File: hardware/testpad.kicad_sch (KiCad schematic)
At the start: 51 parts, among them J1 HC-TYPE-C-16P-CB1.6, J3 AFA01-S08FCA-00, SW1 SSSS811101, SW2 SC4823S6-TR, SW3 SC4823S6-TR, SW4 SC4823S6-TR, SW5 SC4823S6-TR, T1 XL4067TS, U1 ESP32-C6-WROOM-1-N8, U2 BQ24074RGTR, U3 TLA2518IRTER, U6 TPS62142RGTR

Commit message: :bug: improve hardware design
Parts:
- removed R2, R4: 4.7kΩ, KeysDock:R_0402, symbol components:0402,4.7kΩ
- added C12: 1uF, KeysDock:C_0402, symbol components:0402,1uF
- added C13: 100nF, KeysDock:C_0402, symbol components:0402,100nF
- added R15, R16, R18, R25: 10kΩ, KeysDock:R_0402, symbol components:0402,10kΩ
- added R17, R19, R20, R21, R26, R27: 100kΩ, KeysDock:R_0402, symbol components:0402,100kΩ
- added R2, R4: 5.1kΩ, KeysDock:R_0402, symbol components:0402,5.1kΩ
- added R22, R23: 22Ω, KeysDock:R_0402, symbol components:0402,22Ω
- added R24: 47kΩ, KeysDock:R_0402, symbol components:0402,47kΩ
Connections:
- net BAT_CHG: now also R17.2
- net BOOT_0: now also R25.2
- net BOOT_1: now also R16.2
- net EN: now also C12.1, R15.2
- net P,+3.3: now also R15.1, R16.1, R17.1, R18.1, R25.1, R26.1; no longer T1.16 (Y15), T1.17 (Y14), T1.18 (Y13), T1.19 (Y12), T1.2 (Y7), T1.20 (Y11), T1.21 (Y10), T1.22 (Y9), T1.23 (Y8), T1.3 (Y6), T1.4 (Y5), T1.5 (Y4), U3.2 (AIN3/GPIO3), U3.3 (AIN4/GPIO4), U3.4 (AIN5/GPIO5), U3.5 (AIN6/GPIO6)
- net P,E: now also C12.2, R19.2, R2.2, R24.1, R4.2; no longer U2.14 (TMR)
- net P,GND: now also C13.2, R21.1, R27.2
- net RANA: now also R19.1
- net SAKI_MOVE: now also R18.2
- net USB_D+: now also R22.2; no longer J1.A6 (D+), J1.B6 (D+)
- net USB_D-: now also R23.2; no longer J1.A7 (D-), J1.B7 (D-)
- net VBAT: now also R20.1; no longer U3.6 (AIN7/GPIO7)
- net BAT_PGOOD: now reaches U2.7 (~{PGOOD})
- net BAT_PGOOD: now also U1.4 (MTMS/GPIO4/ADC1_CH4)
- net at J1.A5 (CC1): now also R4.1
- net at J1.B5 (CC2): now also R2.1
- new net: R24.2, U2.14 (TMR)
- new net: C13.1, R20.2, R21.2, U3.6 (AIN7/GPIO7)
- new net: J1.A6 (D+), J1.B6 (D+), R22.1
- new net: J1.A7 (D-), J1.B7 (D-), R23.1
- new net KEYS_DT_OTHER: R26.2, R27.1, T1.16 (Y15), T1.17 (Y14), T1.18 (Y13), T1.19 (Y12), T1.2 (Y7), T1.20 (Y11), T1.21 (Y10), T1.22 (Y9), T1.23 (Y8), T1.3 (Y6), T1.4 (Y5), T1.5 (Y4), U3.2 (AIN3/GPIO3), U3.3 (AIN4/GPIO4), U3.4 (AIN5/GPIO5), U3.5 (AIN6/GPIO6)
- no-connect marks 5 -> 3
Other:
- moved on the sheet: LED2, LED3, LED4, LED5, R14, T1

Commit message: :sparkles: sync testpad
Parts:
- removed R17: 100kΩ, KeysDock:R_0402, symbol components:0402,100kΩ
- removed R25: 10kΩ, KeysDock:R_0402, symbol components:0402,10kΩ
- added D2: TPD1E10B06DPYR, KeysDock:DIO_TPD1E05U06DPYR, symbol components:TPD1E10B06DPYR
- added R17, R25: 1.5kΩ, KeysDock:R_0402, symbol components:0402,1.5kΩ
- added R28: 10kΩ, KeysDock:R_0402, symbol components:0402,10kΩ
- added U4: TPD4E05U06DQAR, KeysDock:IC_TPD4E05U06DQAR, symbol components:TPD4E05U06DQAR
- L1: value 2.2uH,5mA -> 2.2uH,3A
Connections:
- net BAT_CHG: now also R17.2
- net BAT_PGOOD: now also R25.2
- net BOOT_0: now also R28.2
- net P,+3.3: now also R28.1
- net P,+5: now also R17.1, R25.1
- net USB_PWR_SUPP: now also D2.1
- net at J1.B5 (CC2), R2.1: now also U4.5 (D2-)
- net at J1.A5 (CC1), R4.1: now also U4.1 (D1+)
- net at J1.A6 (D+), J1.B6 (D+), R22.1: now also U4.10 (NC_10), U4.2 (D1-), U4.9 (NC_9)
- net at J1.A7 (D-), J1.B7 (D-), R23.1: now also U4.4 (D2+), U4.6 (NC_6), U4.7 (NC_7)
- net P,E renamed GND
- net GND: now also D2.2, U4.3 (GND), U4.8 (GND)
- no-connect marks 3 -> 5
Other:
- moved on the sheet: LED2, LED3, LED4, LED5, R14, R26, R27, T1

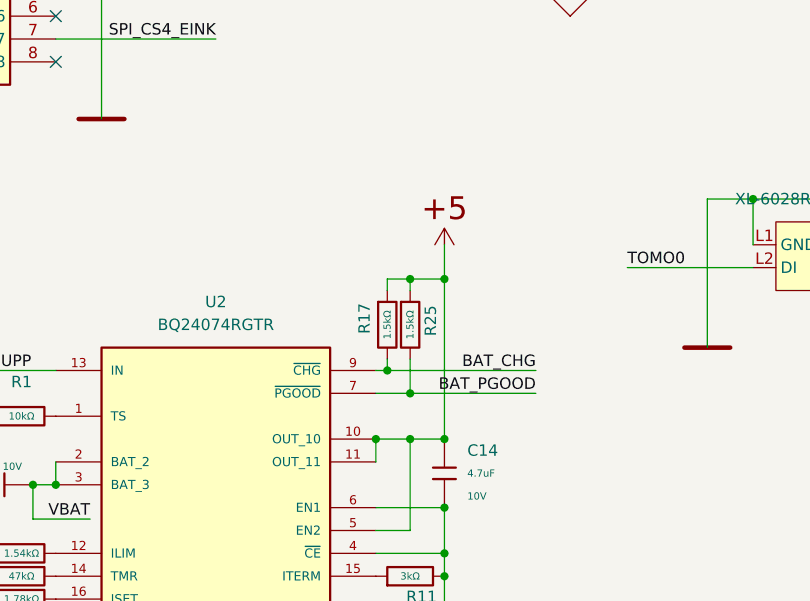
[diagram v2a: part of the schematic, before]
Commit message: :zap: improve led power supply
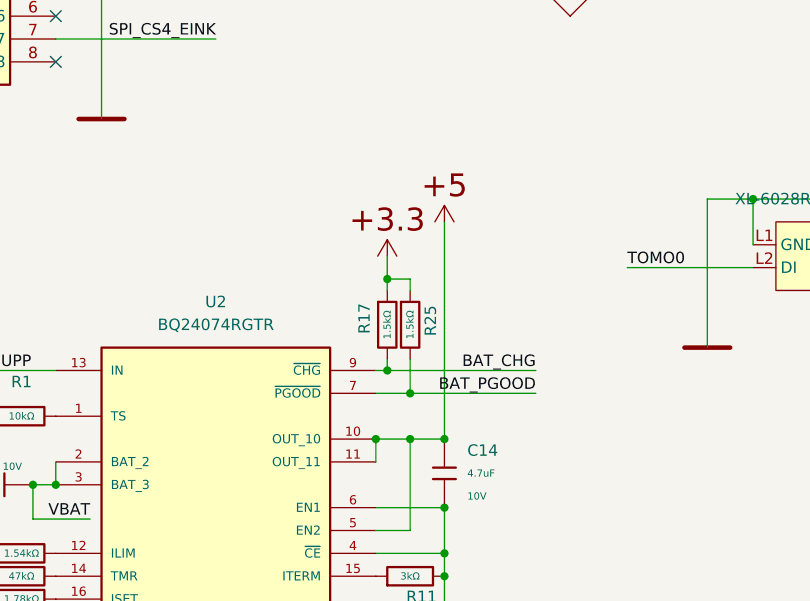
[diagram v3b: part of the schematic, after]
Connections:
- net P,+3.3: now also R17.1, R25.1
- net P,+5: no longer R17.1, R25.1
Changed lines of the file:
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@@
 	)
 	(junction
+		(at 242.57 219.71)
+		(diameter 0)
+		(color 0 0 0 0)
+	)
+	(junction
 		(at 148.59 208.28)
 		(diameter 0)
@@
 	)
 	(junction
+		(at 248.92 237.49)
+		(diameter 0)
+		(color 0 0 0 0)
+	)
+	(junction
 		(at 71.12 222.25)
 		(diameter 0)
@@
 	)
 	(junction
-		(at 248.92 219.71)
-		(diameter 0)
-		(color 0 0 0 0)
-	)
-	(junction
 		(at 151.13 27.94)
 		(diameter 0)
@@
 	)
 	(junction
-		(at 248.92 237.49)
-		(diameter 0)
-		(color 0 0 0 0)
-	)
-	(junction
 		(at 120.65 203.2)
 		(diameter 0)
@@
 	)
 	(junction
-		(at 245.11 219.71)
-		(diameter 0)
-		(color 0 0 0 0)
-	)
-	(junction
 		(at 55.88 233.68)
 		(diameter 0)
@@
 	(wire
 		(pts
-			(xy 245.11 219.71) (xy 248.92 219.71)
-		)
-		(stroke
-			(width 0)
-			(type default)
-		)
-	)
-	(wire
-		(pts
 			(xy 269.24 218.44) (xy 283.21 218.44)
 		)
@@
 	(wire
 		(pts
-			(xy 248.92 215.9) (xy 248.92 219.71)
+			(xy 139.7 76.2) (xy 157.48 76.2)
 		)
 		(stroke
@@
 	(wire
 		(pts
-			(xy 139.7 76.2) (xy 157.48 76.2)
+			(xy 248.92 213.36) (xy 248.92 237.49)
 		)
 		(stroke
@@
 	(wire
 		(pts
-			(xy 248.92 219.71) (xy 248.92 237.49)
+			(xy 226.06 161.29) (xy 231.14 161.29)
 		)
 		(stroke
@@
 	(wire
 		(pts
-			(xy 226.06 161.29) (xy 231.14 161.29)
+			(xy 242.57 217.17) (xy 242.57 219.71)
 		)
 		(stroke
@@
 	)
 	(symbol
+		(lib_id "PCM_Generic:P,+3.3")
+		(at 242.57 217.17 0)
+		(unit 1)
+		(body_style 1)
+		(exclude_from_sim no)
+		(in_bom yes)
+		(on_board yes)
+		(in_pos_files yes)
+		(dnp no)
+		(fields_autoplaced yes)
+		(property "Reference" "#PWR057"
+			(at 245.11 217.17 0)
+			(hide yes)
+			(show_name no)
+			(do_not_autoplace no)
+			(effects
+				(font
+					(size 2.54 2.54)
+				)
+				(justify left)
+			)
+		)
+		(property "Value" "P,+3.3"
+			(at 242.57 214.63 0)
+			(hide yes)
+			(show_name no)
+			(do_not_autoplace no)
+			(effects
+				(font
+					(size 0.001 0.001)
+				)
+				(justify bottom)
+			)
+		)
+		(property "Footprint" ""
+			(at 242.57 217.17 0)
+			(hide yes)
+			(show_name no)
+			(do_not_autoplace no)
+			(effects
+				(font
+					(size 2.54 2.54)
+				)
+			)
+		)
+		(property "Datasheet" ""
+			(at 242.57 217.17 0)
+			(hide yes)
+			(show_name no)
+			(do_not_autoplace no)
+			(effects
+				(font
+					(size 2.54 2.54)
+				)
+			)
+		)
+		(property "Description" "+3.3 positive potential/voltage (global DC power supply node)"
+			(at 242.57 217.17 0)
+			(hide yes)
+			(show_name no)
+			(do_not_autoplace no)
+			(effects
+				(font
+					(size 1.27 1.27)
+				)
+			)
+		)
+		(pin "0"
+		)
+		(instances
+			(project "testpad"
+				(path "/4162c9f0-7325-4010-974e-29020dac9fdc"
+					(reference "#PWR057")
+					(unit 1)
+				)
+			)
+		)
+	)
+	(symbol
 		(lib_id "components:EC12E1240301")
 		(at 168.91 38.1 270)
@@
 	(symbol
 		(lib_id "PCM_Generic:P,+5")
-		(at 248.92 215.9 0)
+		(at 248.92 213.36 0)
 		(unit 1)
 		(body_style 1)
@@
 		(fields_autoplaced yes)
 		(property "Reference" "#PWR031"
-			(at 251.46 215.9 0)
+			(at 251.46 213.36 0)
 			(hide yes)
 			(show_name no)
@@
 		)
 		(property "Value" "P,+5"
-			(at 248.92 213.36 0)
+			(at 248.92 210.82 0)
 			(hide yes)
 			(show_name no)
@@
 		)
 		(property "Footprint" ""
-			(at 248.92 215.9 0)
+			(at 248.92 213.36 0)
 			(hide yes)
 			(show_name no)
@@
 		)
 		(property "Datasheet" ""
-			(at 248.92 215.9 0)
+			(at 248.92 213.36 0)
 			(hide yes)
 			(show_name no)
@@
 		)
 		(property "Description" "+5 positive potential/voltage (global DC power supply node)"
-			(at 248.92 215.9 0)
+			(at 248.92 213.36 0)
 			(hide yes)
 			(show_name no)

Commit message: :sparkles: change to TYPE-C 16P CB1.2
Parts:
- removed J1: HC-TYPE-C-16P-CB1.6, KeysDock:HC-TYPE-C-16P-CB1.6, symbol components:HC-TYPE-C-16P-CB1.6
- removed R7: 1.78kΩ, KeysDock:R_0402, symbol components:0402,1.78kΩ
- removed R8: 1.54kΩ, KeysDock:R_0402, symbol components:0402,1.54kΩ
- added C16: 1uF, KeysDock:C_0402, symbol components:0402,1uF
- added C17: 10uF, KeysDock:C_0402, symbol components:0402,10uF
- added J1: TYPE-C 16PFS 2JCB1.2-H6.5 IPX8, KeysDock:USB-C-SMD_SHOUHAN_TYPE-C-16PFS-2JCB1.2-H6.5, symbol components:TYPE-C16PFS2JCB1.2-H6.5IPX8
- added R29: 10kΩ, KeysDock:R_0402, symbol components:0402,10kΩ
- added R7: 750Ω, KeysDock:R_0402, symbol components:0402,750Ω
- added R8: 1.10kΩ, KeysDock:R_0402, symbol components:0402,1.10kΩ
- added U5: TPS22910AYZVR, KeysDock:BGA4N50P2X2_88X88X50N, symbol components:TPS22910AYZVR
- L1: value 2.2uH,3A -> 2.2uH; Inductance 22uH -> 2.2uH; LCSC Part (none) -> C5832372; Manufacturer cjiang -> cjiang (Changjiang Microelectronics Tech); Rated Current 3.8A -> 3A; Saturation Current (Isat) (none) -> 3.8A; Type (none) -> Molding Choke
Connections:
- net BOOT_0: now also R29.2; no longer R28.2
- net GND: now also S2.D (GND), S2.E (GND), U2.5 (EN2), C16.1, C17.1, J1.13 (EH), J1.B12A1 (GND), J1.B1A12 (GND), R7.1, R8.1, U5.B1 (GND); no longer U2.6 (EN1)
- net P,+3.3: now also R29.1; no longer R28.1
- net P,+5: now also C16.2, U5.A1 (VOUT); no longer C14.2, C8.1, U2.10 (OUT_10), U2.11 (OUT_11), U2.5 (EN2), U6.10 (AVIN), U6.11 (PVIN_11), U6.12 (PVIN_12), U6.13 (EN)
- net USB_PWR_SUPP: now also R28.2, J1.A4B9 (VBUS), J1.A9B4 (VBUS)
- net at R2.1, U4.5 (D2-): now also J1.B5 (CC2)
- net at R4.1, U4.1 (D1+): now also J1.A5 (CC1)
- net at R22.1, U4.10 (NC_10), U4.2 (D1-)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: now also J1.A6 (DP1), J1.B6 (DP2)
- net at R23.1, U4.4 (D2+), U4.6 (NC_6)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: now also J1.A7 (DN1), J1.B7 (DN2)
- net at U2.12 (ILIM): now also R8.2
- net at U2.16 (ISET): now also R7.2
- net BOOT_1 renamed BOOT_1/LED_ON
- net BOOT_1/LED_ON: now also U5.B2 (ON)
- new net: R28.1, U2.6 (EN1)
- new net P,+: C14.2, C17.2, C8.1, U2.10 (OUT_10), U2.11 (OUT_11), U5.A2 (VIN), U6.10 (AVIN), U6.11 (PVIN_11), U6.12 (PVIN_12), U6.13 (EN)
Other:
- note added: "NOTE: P,+ is the original high voltage from BAT/USB power -> BQ24074, it will be connected to P,+5 when the LED system is power-on. the P,+5 network is only used for LED power supply."
- moved on the sheet: LED2, LED3, LED4, LED5, R14, R26, R27, T1
